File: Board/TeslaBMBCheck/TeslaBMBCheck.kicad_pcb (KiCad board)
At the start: 2 copper layers, 99.4 x 60.2 mm, 35 parts, among them J1 TESLA_BMS, J9 ICSP, Q1 IRLML2244, Q2 BSS138, U1 USBLC6, U2 PIC18F2480-ISO, Y1 10 MHz

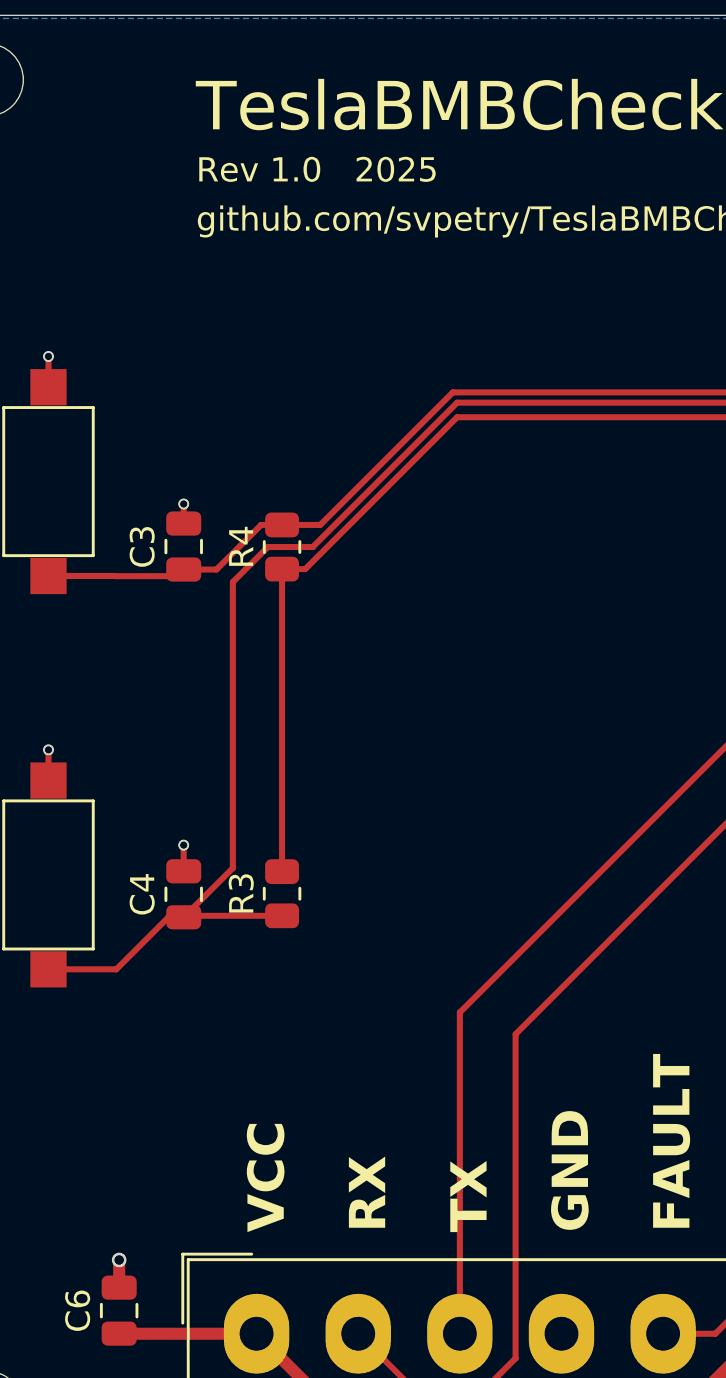
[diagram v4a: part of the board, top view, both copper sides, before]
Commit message: Fixes swapped RX/TX. Changes R10 value
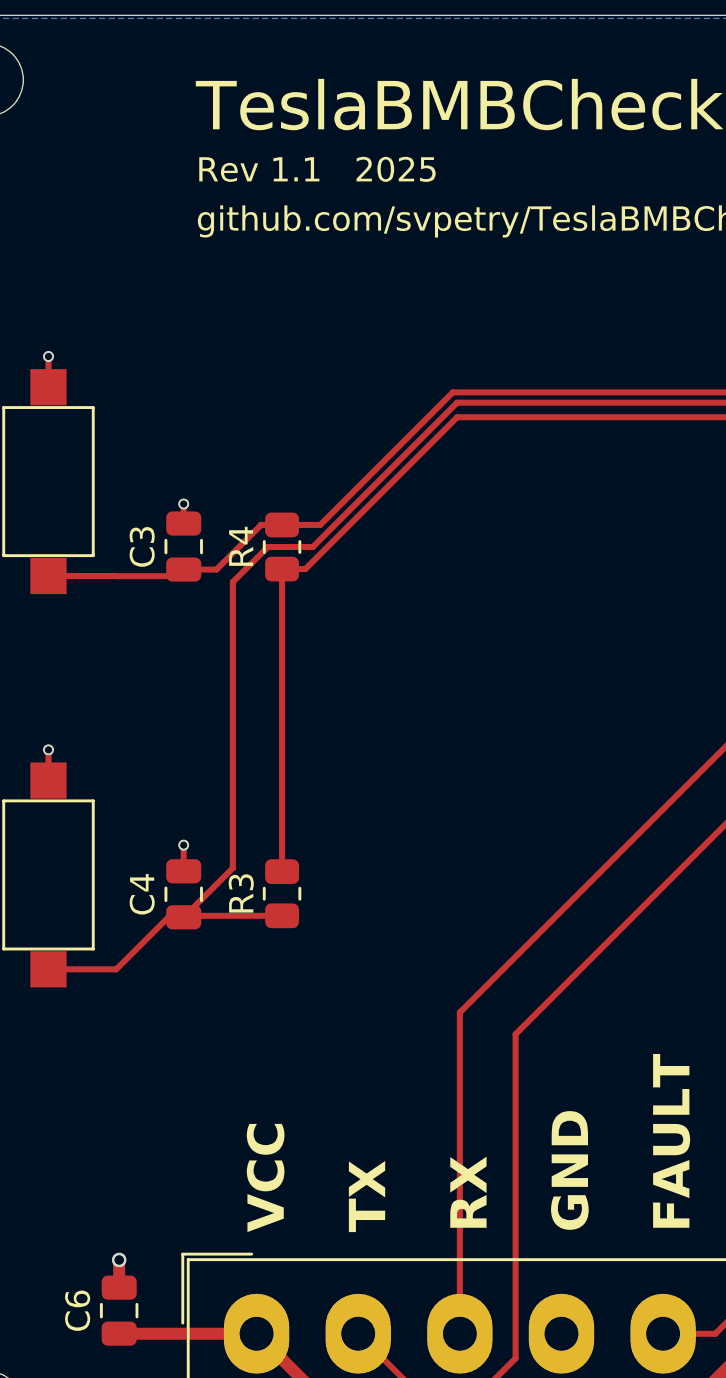
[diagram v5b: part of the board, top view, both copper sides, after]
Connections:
- J1 pad 2: /BMS_RX -> /BMS_TX
- J1 pad 3: /BMS_TX -> /BMS_RX
- U1 pad 1: /BMS_TX -> /BMS_RX
- U1 pad 3: /BMS_RX -> /BMS_TX
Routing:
- net /BMS_TX: track 47.3 -> 52.8 mm
- net /BMS_RX: track 52.8 -> 47.3 mm
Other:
- board text added: "Rev 1.1 2025"
- board text removed: "Rev 1.0 2025"
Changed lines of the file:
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@@
 	(title_block
 		(title "TeslaBMBChecker")
-		(date "2025-07-11")
-		(rev "1.0")
+		(date "2025-07-26")
+		(rev "1.1")
 	)
 	(layers
@@
 			(layers "F.Cu" "F.Mask" "F.Paste")
 			(roundrect_rratio 0.25)
-			(net 17 "/BMS_TX")
+			(net 16 "/BMS_RX")
 			(pinfunction "I/O1")
 			(pintype "passive")
@@
 			(layers "F.Cu" "F.Mask" "F.Paste")
 			(roundrect_rratio 0.25)
-			(net 16 "/BMS_RX")
+			(net 17 "/BMS_TX")
 			(pinfunction "I/O2")
 			(pintype "passive")
@@
 			(layers "*.Cu" "*.Mask")
 			(remove_unused_layers no)
-			(net 16 "/BMS_RX")
+			(net 17 "/BMS_TX")
 			(pinfunction "Pin_2")
 			(pintype "passive")
@@
 			(layers "*.Cu" "*.Mask")
 			(remove_unused_layers no)
-			(net 17 "/BMS_TX")
+			(net 16 "/BMS_RX")
 			(pinfunction "Pin_3")
 			(pintype "passive")
@@
 	)
 	(gr_text "TX"
-		(at 99.06 97.917 90)
+		(at 94.869 97.917 90)
 		(layer "F.SilkS")
 		(effects
@@
 	)
 	(gr_text "RX"
-		(at 94.869 97.917 90)
+		(at 99.06 97.917 90)
 		(layer "F.SilkS")
 		(effects
@@
 		)
 	)
-	(gr_text "Rev 1.0   2025"
+	(gr_text "Rev 1.1   2025"
 		(at 86.868 54.61 0)
 		(layer "F.SilkS")
@@
 	)
 	(segment
-		(start 100.076 103.124)
-		(end 98.552 104.648)
+		(start 97.772 102.108)
+		(end 97.772 88.830057)
 		(width 0.25)
 		(layer "F.Cu")
@@
 	)
 	(segment
-		(start 98.552 104.648)
-		(end 96.112 104.648)
+		(start 120.877057 65.725)
+		(end 122.1795 65.725)
 		(width 0.25)
 		(layer "F.Cu")
@@
 	)
 	(segment
-		(start 96.112 104.648)
-		(end 93.572 102.108)
+		(start 97.772 88.830057)
+		(end 120.877057 65.725)
 		(width 0.25)
 		(layer "F.Cu")
@@
 	)
 	(segment
-		(start 100.076 89.7285)
-		(end 100.076 103.124)
+		(start 100.076 103.124)
+		(end 98.552 104.648)
 		(width 0.25)
 		(layer "F.Cu")
-		(net 16)
+		(net 17)
 	)
 	(segment
-		(start 122.1795 67.625)
-		(end 100.076 89.7285)
+		(start 98.552 104.648)
+		(end 96.112 104.648)
 		(width 0.25)
 		(layer "F.Cu")
-		(net 16)
+		(net 17)
 	)
 	(segment
-		(start 97.772 102.108)
-		(end 97.772 88.830057)
+		(start 96.112 104.648)
+		(end 93.572 102.108)
 		(width 0.25)
 		(layer "F.Cu")
@@
 	)
 	(segment
-		(start 120.877057 65.725)
-		(end 122.1795 65.725)
+		(start 100.076 89.7285)
+		(end 100.076 103.124)
 		(width 0.25)
 		(layer "F.Cu")
@@
 	)
 	(segment
-		(start 97.772 88.830057)
-		(end 120.877057 65.725)
+		(start 122.1795 67.625)
+		(end 100.076 89.7285)
 		(width 0.25)
 		(layer "F.Cu")

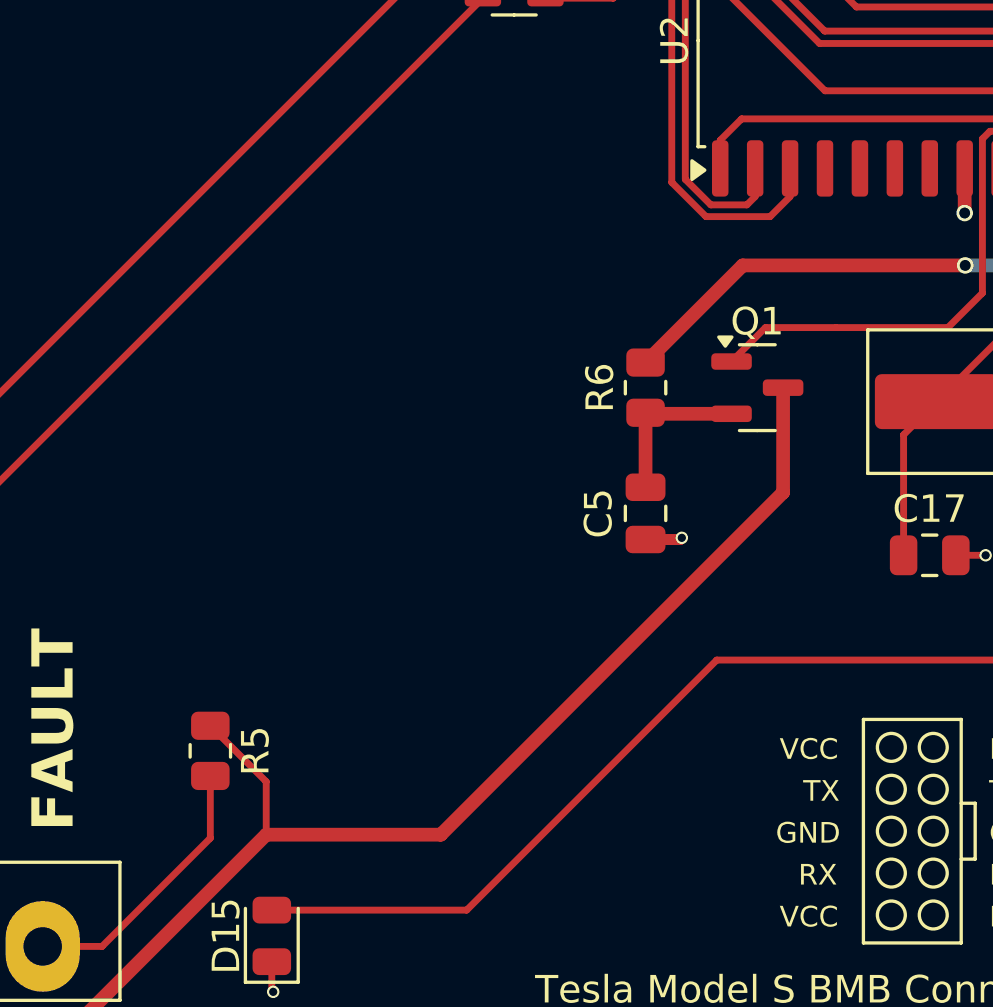
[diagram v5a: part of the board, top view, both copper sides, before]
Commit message: Adds fault detection and clearing.
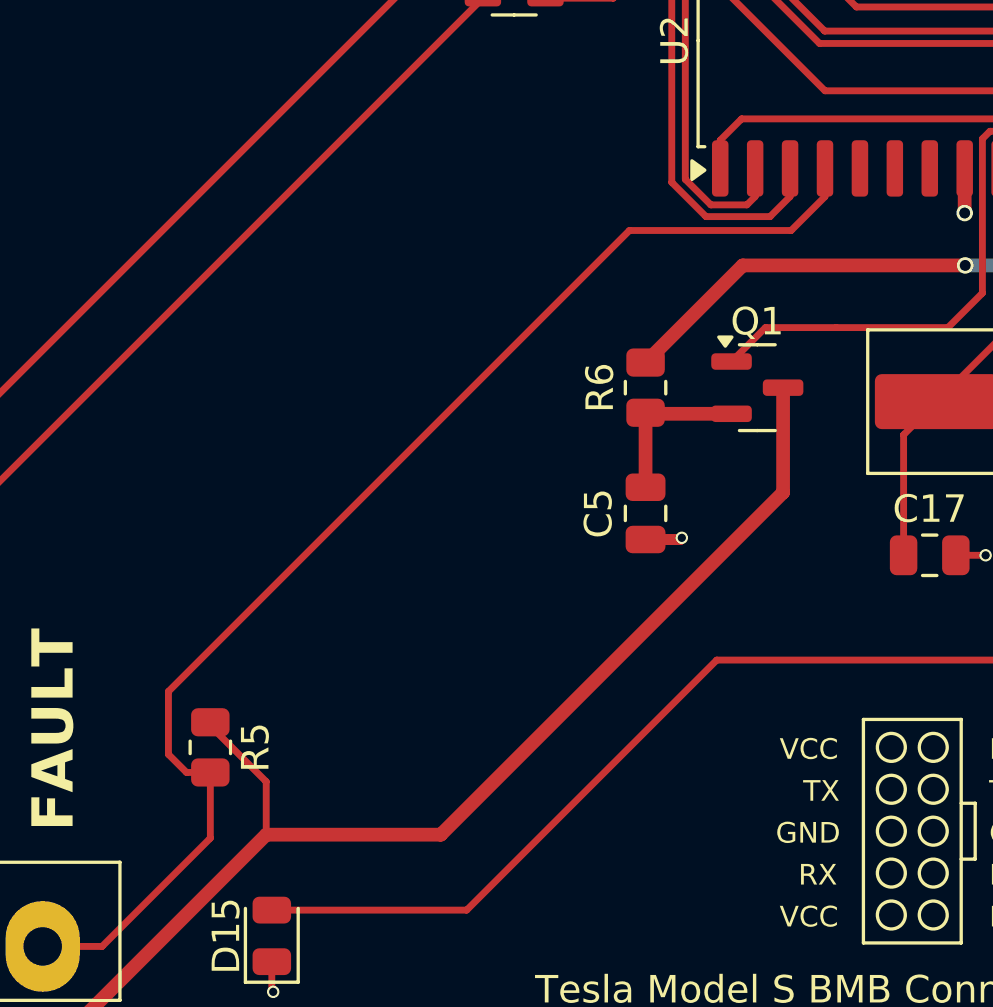
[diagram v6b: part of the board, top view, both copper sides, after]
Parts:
- R10: value 22K -> 15K
- moved R5 0.13 mm to (112.3, 94.9)
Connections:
- J1 pad 5: /BMS_FAULT -> BMS_FAULT
- R5 pad 2: /BMS_FAULT -> BMS_FAULT
- U2 pad 4: unconnected-(U2-RA2/AN2/Vref--Pad4) -> BMS_FAULT
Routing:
- net BMS_FAULT: track 0.00 -> 46.6 mm
- net /BMS_FAULT: track 9.99 -> 0.00 mm
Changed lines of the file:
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@@
 	(net 16 "/BMS_RX")
 	(net 17 "/BMS_TX")
-	(net 18 "/BMS_FAULT")
+	(net 18 "BMS_FAULT")
 	(net 19 "/BMS_VCC")
 	(net 20 "/PGD")
@@
 	(net 28 "/RX")
 	(net 29 "/TX")
-	(net 30 "unconnected-(U2-RA2{slash}AN2{slash}Vref--Pad4)")
-	(net 31 "unconnected-(U2-RA3{slash}AN3{slash}Vref+-Pad5)")
-	(net 32 "unconnected-(U2-RA4{slash}T0CKI-Pad6)")
-	(net 33 "unconnected-(U2-SCL{slash}SCK{slash}RC3-Pad14)")
-	(net 34 "unconnected-(U2-SDI{slash}SDA{slash}RC4-Pad15)")
-	(net 35 "unconnected-(U2-RA5{slash}AN4{slash}~{SS}{slash}HLVDIN-Pad7)")
-	(net 36 "unconnected-(U2-SDO{slash}RC5-Pad16)")
-	(net 37 "unconnected-(USB1-DP2-Pad8)")
-	(net 38 "unconnected-(USB1-DP1-Pad6)")
-	(net 39 "unconnected-(USB1-DN2-Pad5)")
-	(net 40 "unconnected-(USB1-SBU2-Pad3)")
-	(net 41 "unconnected-(USB1-DN1-Pad7)")
-	(net 42 "unconnected-(USB1-SBU1-Pad9)")
-	(net 43 "Net-(D15-A)")
-	(net 44 "Net-(U2-CCP1{slash}RC2)")
+	(net 30 "unconnected-(U2-RA3{slash}AN3{slash}Vref+-Pad5)")
+	(net 31 "unconnected-(U2-RA4{slash}T0CKI-Pad6)")
+	(net 32 "unconnected-(U2-SCL{slash}SCK{slash}RC3-Pad14)")
+	(net 33 "unconnected-(U2-SDI{slash}SDA{slash}RC4-Pad15)")
+	(net 34 "unconnected-(U2-RA5{slash}AN4{slash}~{SS}{slash}HLVDIN-Pad7)")
+	(net 35 "unconnected-(U2-SDO{slash}RC5-Pad16)")
+	(net 36 "unconnected-(USB1-DP2-Pad8)")
+	(net 37 "unconnected-(USB1-DP1-Pad6)")
+	(net 38 "unconnected-(USB1-DN2-Pad5)")
+	(net 39 "unconnected-(USB1-SBU2-Pad3)")
+	(net 40 "unconnected-(USB1-DN1-Pad7)")
+	(net 41 "unconnected-(USB1-SBU1-Pad9)")
+	(net 42 "Net-(D15-A)")
+	(net 43 "Net-(U2-CCP1{slash}RC2)")
 	(footprint "Package_TO_SOT_SMD:SOT-23"
 		(layer "F.Cu")
@@
 			(layers "F.Cu" "F.Mask" "F.Paste")
 			(roundrect_rratio 0.25)
-			(net 43 "Net-(D15-A)")
+			(net 42 "Net-(D15-A)")
 			(pinfunction "A")
 			(pintype "passive")
@@
 			)
 		)
-		(property "Value" "22K"
+		(property "Value" "15K"
 			(at 0 1.65 90)
 			(layer "F.Fab")
@@
 			(layers "F.Cu" "F.Mask" "F.Paste")
 			(roundrect_rratio 0.243902)
-			(net 44 "Net-(U2-CCP1{slash}RC2)")
+			(net 43 "Net-(U2-CCP1{slash}RC2)")
 			(pintype "passive")
 		)
@@
 			(layers "F.Cu" "F.Mask" "F.Paste")
 			(roundrect_rratio 0.243902)
-			(net 43 "Net-(D15-A)")
+			(net 42 "Net-(D15-A)")
 			(pintype "passive")
 		)
@@
 	(footprint "Resistor_SMD:R_0805_2012Metric"
 		(layer "F.Cu")
-		(at 112.268 94.996 -90)
+		(at 112.268 94.869 -90)
 		(descr "Resistor SMD 0805 (2012 Metric), square (rectangular) end terminal, IPC-7351 nominal, (Body size source: IPC-SM-782 page 72, https://www.pcb-3d.com/wordpress/wp-content/uploads/ipc-sm-782a_amendment_1_and_2.pdf), generated with kicad-footprint-generator")
 		(tags "resistor")
@@
 			(layers "F.Cu" "F.Mask" "F.Paste")
 			(roundrect_rratio 0.243902)
-			(net 18 "/BMS_FAULT")
+			(net 18 "BMS_FAULT")
 			(pintype "passive")
 		)
@@
 			(layers "*.Cu" "*.Mask")
 			(remove_unused_layers no)
-			(net 18 "/BMS_FAULT")
+			(net 18 "BMS_FAULT")
 			(pinfunction "Pin_5")
 			(pintype "passive")
@@
 			(layers "F.Cu" "F.Mask" "F.Paste")
 			(roundrect_rratio 0.25)
-			(net 30 "unconnected-(U2-RA2{slash}AN2{slash}Vref--Pad4)")
+			(net 18 "BMS_FAULT")
 			(pinfunction "RA2/AN2/Vref-")
-			(pintype "bidirectional+no_connect")
+			(pintype "bidirectional")
 		)
 		(pad "5" smd roundrect
@@
 			(layers "F.Cu" "F.Mask" "F.Paste")
 			(roundrect_rratio 0.25)
-			(net 31 "unconnected-(U2-RA3{slash}AN3{slash}Vref+-Pad5)")
+			(net 30 "unconnected-(U2-RA3{slash}AN3{slash}Vref+-Pad5)")
 			(pinfunction "RA3/AN3/Vref+")
 			(pintype "bidirectional+no_connect")
@@
 			(layers "F.Cu" "F.Mask" "F.Paste")
 			(roundrect_rratio 0.25)
-			(net 32 "unconnected-(U2-RA4{slash}T0CKI-Pad6)")
+			(net 31 "unconnected-(U2-RA4{slash}T0CKI-Pad6)")
 			(pinfunction "RA4/T0CKI")
 			(pintype "bidirectional+no_connect")
@@
 			(layers "F.Cu" "F.Mask" "F.Paste")
 			(roundrect_rratio 0.25)
-			(net 35 "unconnected-(U2-RA5{slash}AN4{slash}~{SS}{slash}HLVDIN-Pad7)")
+			(net 34 "unconnected-(U2-RA5{slash}AN4{slash}~{SS}{slash}HLVDIN-Pad7)")
 			(pinfunction "RA5/AN4/~{SS}/HLVDIN")
 			(pintype "bidirectional+no_connect")
@@
 			(layers "F.Cu" "F.Mask" "F.Paste")
 			(roundrect_rratio 0.25)
-			(net 44 "Net-(U2-CCP1{slash}RC2)")
+			(net 43 "Net-(U2-CCP1{slash}RC2)")
 			(pinfunction "CCP1/RC2")
 			(pintype "bidirectional")
@@
 			(layers "F.Cu" "F.Mask" "F.Paste")
 			(roundrect_rratio 0.25)
-			(net 33 "unconnected-(U2-SCL{slash}SCK{slash}RC3-Pad14)")
+			(net 32 "unconnected-(U2-SCL{slash}SCK{slash}RC3-Pad14)")
 			(pinfunction "SCL/SCK/RC3")
 			(pintype "bidirectional+no_connect")
@@
 			(layers "F.Cu" "F.Mask" "F.Paste")
 			(roundrect_rratio 0.25)
-			(net 34 "unconnected-(U2-SDI{slash}SDA{slash}RC4-Pad15)")
+			(net 33 "unconnected-(U2-SDI{slash}SDA{slash}RC4-Pad15)")
 			(pinfunction "SDI/SDA/RC4")
 			(pintype "bidirectional+no_connect")
@@
 			(layers "F.Cu" "F.Mask" "F.Paste")
 			(roundrect_rratio 0.25)
-			(net 36 "unconnected-(U2-SDO{slash}RC5-Pad16)")
+			(net 35 "unconnected-(U2-SDO{slash}RC5-Pad16)")
 			(pinfunction "SDO/RC5")
 			(pintype "bidirectional+no_connect")
@@
 			(size 0.3 1.45)
 			(layers "F.Cu" "F.Mask" "F.Paste")
-			(net 40 "unconnected-(USB1-SBU2-Pad3)")
+			(net 39 "unconnected-(USB1-SBU2-Pad3)")
 			(pinfunction "SBU2")
 			(pintype "input+no_connect")
@@
 			(size 0.3 1.45)
 			(layers "F.Cu" "F.Mask" "F.Paste")
-			(net 39 "unconnected-(USB1-DN2-Pad5)")
+			(net 38 "unconnected-(USB1-DN2-Pad5)")
 			(pinfunction "DN2")
 			(pintype "input+no_connect")
@@
 			(size 0.3 1.45)
 			(layers "F.Cu" "F.Mask" "F.Paste")
-			(net 38 "unconnected-(USB1-DP1-Pad6)")
+			(net 37 "unconnected-(USB1-DP1-Pad6)")
 			(pinfunction "DP1")
 			(pintype "input+no_connect")
@@
 			(size 0.3 1.45)
 			(layers "F.Cu" "F.Mask" "F.Paste")
-			(net 41 "unconnected-(USB1-DN1-Pad7)")
+			(net 40 "unconnected-(USB1-DN1-Pad7)")
 			(pinfunction "DN1")
 			(pintype "input+no_connect")
@@
 			(size 0.3 1.45)
 			(layers "F.Cu" "F.Mask" "F.Paste")
-			(net 37 "unconnected-(USB1-DP2-Pad8)")
+			(net 36 "unconnected-(USB1-DP2-Pad8)")
 			(pinfunction "DP2")
 			(pintype "input+no_connect")
@@
 			(size 0.3 1.45)
 			(layers "F.Cu" "F.Mask" "F.Paste")
-			(net 42 "unconnected-(USB1-SBU1-Pad9)")
+			(net 41 "unconnected-(USB1-SBU1-Pad9)")
 			(pinfunction "SBU1")
 			(pintype "input+no_connect")
@@
 	)
 	(segment
+		(start 110.744 92.837)
+		(end 110.744 95.123)
+		(width 0.25)
+		(layer "F.Cu")
+		(net 18)
+	)
+	(segment
+		(start 111.4025 95.7815)
+		(end 112.268 95.7815)
+		(width 0.25)
+		(layer "F.Cu")
+		(net 18)
+	)
+	(segment
+		(start 110.744 95.123)
+		(end 111.4025 95.7815)
+		(width 0.25)
+		(layer "F.Cu")
+		(net 18)
+	)
+	(segment
+		(start 127.508 76.073)
+		(end 110.744 92.837)
+		(width 0.25)
+		(layer "F.Cu")
+		(net 18)
+	)
+	(segment
+		(start 133.387999 76.073)
+		(end 127.508 76.073)
+		(width 0.25)
+		(layer "F.Cu")
+		(net 18)
+	)
+	(segment
 		(start 112.268 98.171)
-		(end 112.268 95.9085)
+		(end 112.268 95.7815)
 		(width 0.25)
 		(layer "F.Cu")
@@
 	)
 	(segment
+		(start 134.62 74.840999)
+		(end 133.387999 76.073)
+		(width 0.25)
+		(layer "F.Cu")
+		(net 18)
+	)
+	(segment
+		(start 134.62 73.816)
+		(end 134.62 74.840999)
+		(width 0.25)
+		(layer "F.Cu")
+		(net 18)
+	)
+	(segment
+		(start 112.268 93.9565)
+		(end 112.268 94.0835)
+		(width 0.25)
+		(layer "F.Cu")
+		(net 19)
+	)
+	(segment
 		(start 114.3 98.044)
 		(end 120.65 98.044)
@@
 	)
 	(segment
+		(start 112.268 94.0835)
+		(end 114.3 96.1155)
+		(width 0.25)
+		(layer "F.Cu")
+		(net 19)
+	)
+	(segment
 		(start 106.68 105.664)
 		(end 114.3 98.044)
@@
 	)
 	(segment
-		(start 112.268 94.0835)
-		(end 114.3 96.1155)
-		(width 0.25)
-		(layer "F.Cu")
-		(net 19)
-	)
-	(segment
 		(start 89.372 102.108)
 		(end 92.928 105.664)
@@
 		(width 0.25)
 		(layer "F.Cu")
-		(net 43)
+		(net 42)
 	)
 	(segment
@@
 		(width 0.25)
 		(layer "F.Cu")
-		(net 43)
+		(net 42)
 	)
 	(segment
@@
 		(width 0.25)
 		(layer "F.Cu")
-		(net 43)
+		(net 42)
 	)
 	(segment
@@
 		(width 0.25)
 		(layer "F.Cu")
-		(net 44)
+		(net 43)
 	)
 	(segment
@@
 		(width 0.25)
 		(layer "F.Cu")
-		(net 44)
+		(net 43)
 	)
 	(segment
@@
 		(width 0.25)
 		(layer "F.Cu")
-		(net 44)
+		(net 43)
 	)
 	(segment
@@
 		(width 0.25)
 		(layer "F.Cu")
-		(net 44)
+		(net 43)
 	)
 	(segment
@@
 		(width 0.25)
 		(layer "F.Cu")
-		(net 44)
+		(net 43)
 	)
 	(zone

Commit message: Layout improvements
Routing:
- net /BMS_TX: track 52.8 -> 54.2 mm
- net /PGD: track 53.1 -> 54.3 mm
- net /PGC: track 50.5 -> 50.0 mm
- net GND: track 26.2 -> 26.0 mm, vias 20 -> 115
- added copper zone on F.Cu, net GND
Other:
- board text added: "PIC18F24xx"
